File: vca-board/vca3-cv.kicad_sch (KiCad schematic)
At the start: 9 parts, among them U2 TL074

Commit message: VCA components linked
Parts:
- C5: footprint (none) -> Capacitor_SMD:C_0603_1608Metric_Pad1.08x0.95mm_HandSolder; LCSC (none) -> C91367
- C6: footprint (none) -> Capacitor_SMD:C_0603_1608Metric_Pad1.08x0.95mm_HandSolder; LCSC (none) -> C76711
- D1: footprint (none) -> Diode_SMD:D_SOD-523; LCSC (none) -> C131797
- D2: footprint (none) -> Diode_SMD:D_SOD-123; LCSC (none) -> C81598
- R11: footprint (none) -> Resistor_SMD:R_0201_0603Metric_Pad0.64x0.40mm_HandSolder; LCSC (none) -> C25811
- R14: footprint (none) -> Resistor_SMD:R_0201_0603Metric_Pad0.64x0.40mm_HandSolder; LCSC (none) -> C25803
- R15: LCSC (none) -> C22775
- R16: LCSC (none) -> C25804
- U2: footprint (none) -> Package_SO:SOIC-14_3.9x8.7mm_P1.27mm; LCSC (none) -> C6963
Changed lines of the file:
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@@
     (property "Reference" "C5" (id 0) (at 83.82 17.78 90))
     (property "Value" "10p" (id 1) (at 83.82 20.32 90))
-    (property "Footprint" "" (id 2) (at 87.63 24.4348 0)
+    (property "Footprint" "Capacitor_SMD:C_0603_1608Metric_Pad1.08x0.95mm_HandSolder" (id 2) (at 87.63 24.4348 0)
       (effects (font (size 1.27 1.27)) hide)
     )
@@
       (effects (font (size 1.27 1.27)) hide)
     )
+    (property "LCSC" "C91367" (id 4) (at 83.82 25.4 0)
+      (effects (font (size 1.27 1.27)) hide)
+    )
     (pin "1")
     (pin "2")
@@
       (effects (font (size 1.27 1.27)) (justify left))
     )
-    (property "Footprint" "" (id 2) (at 256.54 44.45 0)
+    (property "Footprint" "Package_SO:SOIC-14_3.9x8.7mm_P1.27mm" (id 2) (at 256.54 44.45 0)
       (effects (font (size 1.27 1.27)) hide)
     )
     (property "Datasheet" "http://www.ti.com/lit/ds/symlink/tl071.pdf" (id 3) (at 259.08 41.91 0)
+      (effects (font (size 1.27 1.27)) hide)
+    )
+    (property "LCSC" "C6963" (id 4) (at 257.81 46.99 0)
       (effects (font (size 1.27 1.27)) hide)
     )
@@
       (effects (font (size 1.27 1.27)) hide)
     )
+    (property "LCSC" "C22775" (id 4) (at 99.06 53.34 0)
+      (effects (font (size 1.27 1.27)) hide)
+    )
     (pin "1")
     (pin "2")
@@
       (effects (font (size 1.27 1.27)) (justify right))
     )
-    (property "Footprint" "" (id 2) (at 244.1448 43.18 0)
+    (property "Footprint" "Capacitor_SMD:C_0603_1608Metric_Pad1.08x0.95mm_HandSolder" (id 2) (at 244.1448 43.18 0)
       (effects (font (size 1.27 1.27)) hide)
     )
@@
       (effects (font (size 1.27 1.27)) hide)
     )
+    (property "LCSC" "C76711" (id 4) (at 245.11 46.99 0)
+      (effects (font (size 1.27 1.27)) hide)
+    )
     (pin "1")
     (pin "2")
@@
       (effects (font (size 1.27 1.27)) (justify left))
     )
-    (property "Footprint" "" (id 2) (at 106.68 66.04 0)
+    (property "Footprint" "Diode_SMD:D_SOD-523" (id 2) (at 106.68 66.04 0)
       (effects (font (size 1.27 1.27)) hide)
     )
@@
       (effects (font (size 1.27 1.27)) hide)
     )
+    (property "LCSC" "C131797" (id 4) (at 106.68 66.04 0)
+      (effects (font (size 1.27 1.27)) hide)
+    )
     (pin "1")
     (pin "2")
@@
     )
     (property "Datasheet" "~" (id 3) (at 140.97 60.96 0)
+      (effects (font (size 1.27 1.27)) hide)
+    )
+    (property "LCSC" "C25804" (id 4) (at 140.97 60.96 0)
       (effects (font (size 1.27 1.27)) hide)
     )
@@
     (property "Reference" "U2" (id 0) (at 83.82 43.18 0))
     (property "Value" "TL074" (id 1) (at 83.82 45.72 0))
-    (property "Footprint" "" (id 2) (at 82.55 55.88 0)
+    (property "Footprint" "Package_SO:SOIC-14_3.9x8.7mm_P1.27mm" (id 2) (at 82.55 55.88 0)
       (effects (font (size 1.27 1.27)) hide)
     )
     (property "Datasheet" "http://www.ti.com/lit/ds/symlink/tl071.pdf" (id 3) (at 85.09 58.42 0)
+      (effects (font (size 1.27 1.27)) hide)
+    )
+    (property "LCSC" "C6963" (id 4) (at 83.82 53.34 0)
       (effects (font (size 1.27 1.27)) hide)
     )
@@
     (property "Reference" "D2" (id 0) (at 134.62 44.45 0))
     (property "Value" "D" (id 1) (at 134.62 46.99 0))
-    (property "Footprint" "" (id 2) (at 134.62 50.8 0)
+    (property "Footprint" "Diode_SMD:D_SOD-123" (id 2) (at 134.62 50.8 0)
       (effects (font (size 1.27 1.27)) hide)
     )
     (property "Datasheet" "~" (id 3) (at 134.62 50.8 0)
+      (effects (font (size 1.27 1.27)) hide)
+    )
+    (property "LCSC" "C81598" (id 4) (at 134.62 50.8 0)
       (effects (font (size 1.27 1.27)) hide)
     )
@@
     (property "Reference" "R11" (id 0) (at 68.58 44.45 90))
     (property "Value" "200k" (id 1) (at 68.58 46.99 90))
-    (property "Footprint" "" (id 2) (at 68.58 52.578 90)
+    (property "Footprint" "Resistor_SMD:R_0201_0603Metric_Pad0.64x0.40mm_HandSolder" (id 2) (at 68.58 52.578 90)
       (effects (font (size 1.27 1.27)) hide)
     )
     (property "Datasheet" "~" (id 3) (at 68.58 50.8 0)
+      (effects (font (size 1.27 1.27)) hide)
+    )
+    (property "LCSC" "C25811" (id 4) (at 68.58 50.8 0)
       (effects (font (size 1.27 1.27)) hide)
     )
@@
     (property "Reference" "R14" (id 0) (at 83.82 31.75 90))
     (property "Value" "100k" (id 1) (at 83.82 34.29 90))
-    (property "Footprint" "" (id 2) (at 83.82 39.878 90)
+    (property "Footprint" "Resistor_SMD:R_0201_0603Metric_Pad0.64x0.40mm_HandSolder" (id 2) (at 83.82 39.878 90)
       (effects (font (size 1.27 1.27)) hide)
     )
     (property "Datasheet" "~" (id 3) (at 83.82 38.1 0)
+      (effects (font (size 1.27 1.27)) hide)
+    )
+    (property "LCSC" "C25803" (id 4) (at 83.82 38.1 0)
       (effects (font (size 1.27 1.27)) hide)
     )
@@
     (property "Reference" "U2" (id 0) (at 119.38 40.64 0))
     (property "Value" "TL074" (id 1) (at 119.38 43.18 0))
-    (property "Footprint" "" (id 2) (at 118.11 53.34 0)
+    (property "Footprint" "Package_SO:SOIC-14_3.9x8.7mm_P1.27mm" (id 2) (at 118.11 53.34 0)
       (effects (font (size 1.27 1.27)) hide)
     )
@@
       (effects (font (size 1.27 1.27)) hide)
     )
+    (property "LCSC" "C6963" (id 4) (at 119.38 50.8 0)
+      (effects (font (size 1.27 1.27)) hide)
+    )

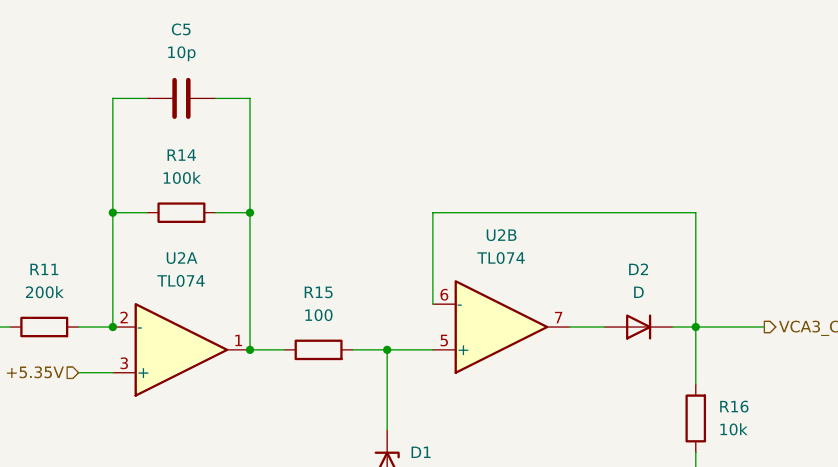
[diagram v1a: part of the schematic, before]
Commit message: VCA board components placed
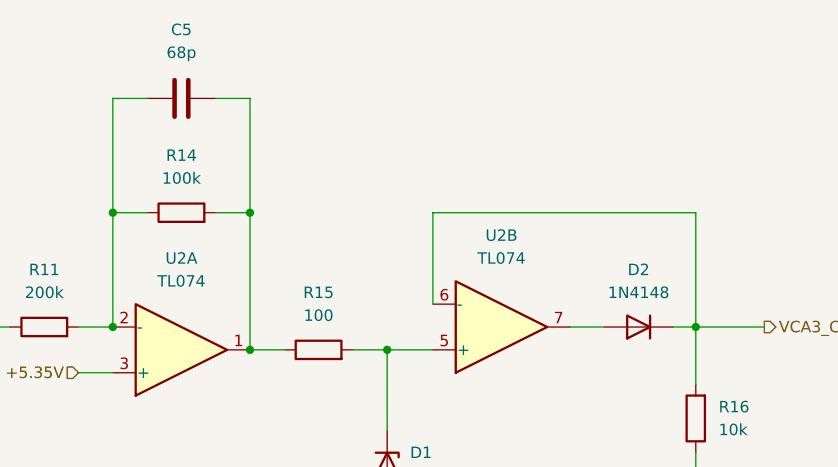
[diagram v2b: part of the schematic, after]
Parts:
- C5: value 10p -> 68p; LCSC C91367 -> C1680
- D1: footprint Diode_SMD:D_SOD-523 -> Diode_SMD:D_SOD-123; LCSC C131797 -> C406712
- D2: value D -> 1N4148
- R11, R14: footprint Resistor_SMD:R_0201_0603Metric_Pad0.64x0.40mm_HandSolder -> Resistor_SMD:R_0603_1608Metric_Pad0.98x0.95mm_HandSolder
- R15, R16: footprint (none) -> Resistor_SMD:R_0603_1608Metric_Pad0.98x0.95mm_HandSolder
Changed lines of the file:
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@@
     (in_bom yes) (on_board yes) (fields_autoplaced)
     (property "Reference" "C5" (id 0) (at 83.82 17.78 90))
-    (property "Value" "10p" (id 1) (at 83.82 20.32 90))
+    (property "Value" "68p" (id 1) (at 83.82 20.32 90))
     (property "Footprint" "Capacitor_SMD:C_0603_1608Metric_Pad1.08x0.95mm_HandSolder" (id 2) (at 87.63 24.4348 0)
       (effects (font (size 1.27 1.27)) hide)
@@
       (effects (font (size 1.27 1.27)) hide)
     )
-    (property "LCSC" "C91367" (id 4) (at 83.82 25.4 0)
+    (property "LCSC" "C1680" (id 4) (at 83.82 25.4 0)
       (effects (font (size 1.27 1.27)) hide)
     )
@@
     (property "Reference" "R15" (id 0) (at 99.06 46.99 90))
     (property "Value" "100" (id 1) (at 99.06 49.53 90))
-    (property "Footprint" "" (id 2) (at 99.06 55.118 90)
+    (property "Footprint" "Resistor_SMD:R_0603_1608Metric_Pad0.98x0.95mm_HandSolder" (id 2) (at 99.06 55.118 90)
       (effects (font (size 1.27 1.27)) hide)
     )
@@
       (effects (font (size 1.27 1.27)) (justify left))
     )
-    (property "Footprint" "Diode_SMD:D_SOD-523" (id 2) (at 106.68 66.04 0)
+    (property "Footprint" "Diode_SMD:D_SOD-123" (id 2) (at 106.68 66.04 0)
       (effects (font (size 1.27 1.27)) hide)
     )
@@
       (effects (font (size 1.27 1.27)) hide)
     )
-    (property "LCSC" "C131797" (id 4) (at 106.68 66.04 0)
+    (property "LCSC" "C406712" (id 4) (at 106.68 66.04 0)
       (effects (font (size 1.27 1.27)) hide)
     )
@@
       (effects (font (size 1.27 1.27)) (justify right))
     )
-    (property "Footprint" "" (id 2) (at 142.748 60.96 90)
+    (property "Footprint" "Resistor_SMD:R_0603_1608Metric_Pad0.98x0.95mm_HandSolder" (id 2) (at 142.748 60.96 90)
       (effects (font (size 1.27 1.27)) hide)
     )
@@
     (in_bom yes) (on_board yes) (fields_autoplaced)
     (property "Reference" "D2" (id 0) (at 134.62 44.45 0))
-    (property "Value" "D" (id 1) (at 134.62 46.99 0))
+    (property "Value" "1N4148" (id 1) (at 134.62 46.99 0))
     (property "Footprint" "Diode_SMD:D_SOD-123" (id 2) (at 134.62 50.8 0)
       (effects (font (size 1.27 1.27)) hide)
@@
     (property "Reference" "R11" (id 0) (at 68.58 44.45 90))
     (property "Value" "200k" (id 1) (at 68.58 46.99 90))
-    (property "Footprint" "Resistor_SMD:R_0201_0603Metric_Pad0.64x0.40mm_HandSolder" (id 2) (at 68.58 52.578 90)
+    (property "Footprint" "Resistor_SMD:R_0603_1608Metric_Pad0.98x0.95mm_HandSolder" (id 2) (at 68.58 52.578 90)
       (effects (font (size 1.27 1.27)) hide)
     )
@@
     (property "Reference" "R14" (id 0) (at 83.82 31.75 90))
     (property "Value" "100k" (id 1) (at 83.82 34.29 90))
-    (property "Footprint" "Resistor_SMD:R_0201_0603Metric_Pad0.64x0.40mm_HandSolder" (id 2) (at 83.82 39.878 90)
+    (property "Footprint" "Resistor_SMD:R_0603_1608Metric_Pad0.98x0.95mm_HandSolder" (id 2) (at 83.82 39.878 90)
       (effects (font (size 1.27 1.27)) hide)
     )

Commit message: wip
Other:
- note added: "Bridge instead of D2 to let the vol go all the way to quiet"
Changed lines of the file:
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@@
     (stroke (width 0) (type default) (color 0 0 0 0))
+  )
+  (text "Bridge instead of D2 to\nlet the vol go all the way to quiet"
+    (at 129.54 31.75 0)
+    (effects (font (size 1.27 1.27)) (justify left bottom))
   )
   (hierarchical_label "+5.35V" (shape input) (at 72.39 55.88 180)

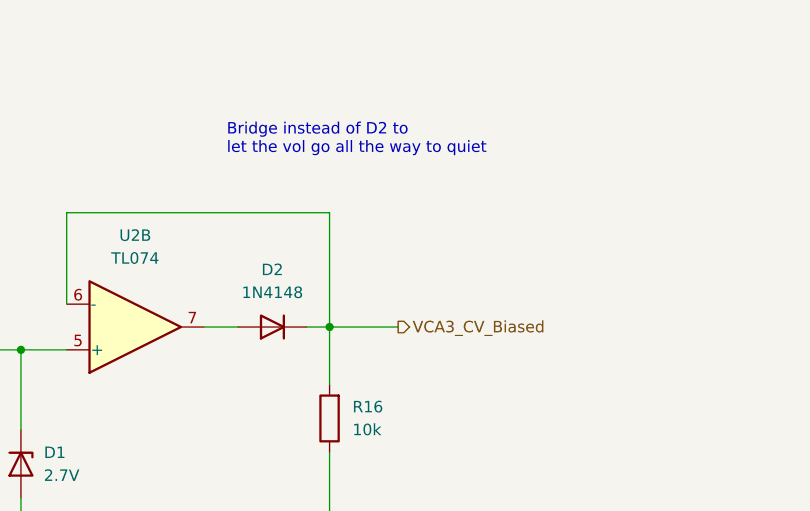
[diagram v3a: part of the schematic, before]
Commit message: Remove D from linear VCA + update graphics
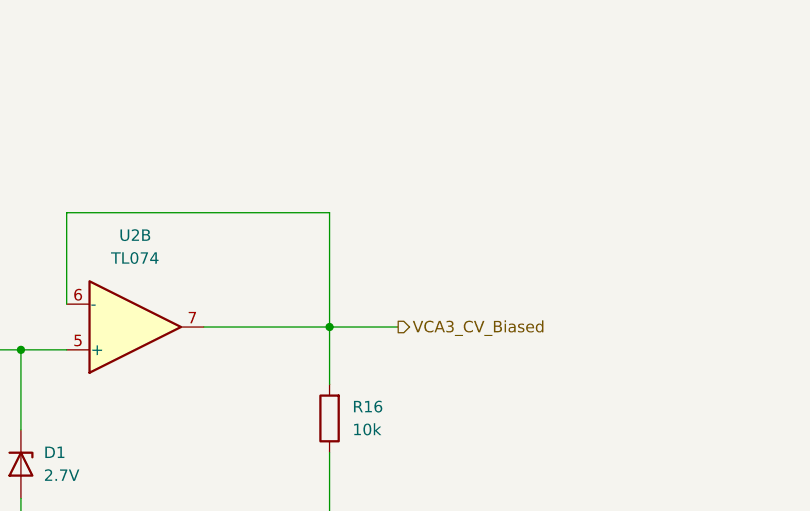
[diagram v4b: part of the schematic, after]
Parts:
- removed D2: 1N4148, Diode_SMD:D_SOD-123, symbol Device:D
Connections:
- net VCA3_CV_Biased: now also U2.7
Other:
- note removed: "Bridge instead of D2 to let the vol go all the way to quiet"
- company: (none) -> Pedal Markt / Andrey Salomatin
- title: (none) -> VCA Board
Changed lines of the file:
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@@
 (kicad_sch (version 20211123) (generator eeschema)
   (paper "A4")
+  (title_block
+    (title "VCA Board")
+    (date "2024-11-07")
+    (rev "v1rev2")
+    (company "Pedal Markt / Andrey Salomatin")
+  )
   (junction (at 91.44 53.34) (diameter 0) (color 0 0 0 0)
   )
@@
     (stroke (width 0) (type default) (color 0 0 0 0))
   )
-  (wire (pts (xy 138.43 50.8) (xy 140.97 50.8))
-    (stroke (width 0) (type default) (color 0 0 0 0))
-  )
   (wire (pts (xy 255.27 33.02) (xy 255.27 39.37))
     (stroke (width 0) (type default) (color 0 0 0 0))
@@
     (stroke (width 0) (type default) (color 0 0 0 0))
   )
-  (wire (pts (xy 127 50.8) (xy 130.81 50.8))
+  (wire (pts (xy 127 50.8) (xy 140.97 50.8))
     (stroke (width 0) (type default) (color 0 0 0 0))
   )
@@
   (wire (pts (xy 106.68 73.66) (xy 106.68 69.85))
     (stroke (width 0) (type default) (color 0 0 0 0))
-  )
-  (text "Bridge instead of D2 to\nlet the vol go all the way to quiet"
-    (at 129.54 31.75 0)
-    (effects (font (size 1.27 1.27)) (justify left bottom))
   )
   (hierarchical_label "+5.35V" (shape input) (at 72.39 55.88 180)
@@
     (pin "4")
   )
-  (symbol (lib_id "Device:D") (at 134.62 50.8 180) (unit 1)
-    (in_bom yes) (on_board yes) (fields_autoplaced)
-    (property "Reference" "D2" (id 0) (at 134.62 44.45 0))
-    (property "Value" "1N4148" (id 1) (at 134.62 46.99 0))
-    (property "Footprint" "Diode_SMD:D_SOD-123" (id 2) (at 134.62 50.8 0)
-      (effects (font (size 1.27 1.27)) hide)
-    )
-    (property "Datasheet" "~" (id 3) (at 134.62 50.8 0)
-      (effects (font (size 1.27 1.27)) hide)
-    )
-    (property "LCSC" "C81598" (id 4) (at 134.62 50.8 0)
-      (effects (font (size 1.27 1.27)) hide)
-    )
-    (pin "1")
-    (pin "2")
-  )
   (symbol (lib_id "Device:R") (at 68.58 50.8 90) (unit 1)

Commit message: wip pre-redo orientation
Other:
- company: Pedal Markt / Andrey Salomatin -> Andrey Salomatin / Pedal Markt
- title: VCA Board -> Mag
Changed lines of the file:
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@@
   (paper "A4")
   (title_block
-    (title "VCA Board")
+    (title "Mag")
     (date "2024-11-07")
     (rev "v1rev2")
-    (company "Pedal Markt / Andrey Salomatin")
+    (company "Andrey Salomatin / Pedal Markt")
   )
   (junction (at 91.44 53.34) (diameter 0) (color 0 0 0 0)
